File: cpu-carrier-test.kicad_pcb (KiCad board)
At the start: 2 copper layers, 99.9 x 103.3 mm, 89 parts, among them J1 Micro_SD_Card_Det, J1101 USB_miniB, J1102 USB_C_Receptacle_USB2.0, J19 SFP, J20 SFP_CAGE, J4 JTAG, J5 Molex_0936263508, J6 USB_A, SW1 SW_Push, U1 TXS0108EPW, U1101 USB3740B-AI9, U1102 UTC2000, U1103 FT232RL, U1104 74LVC1G00, U1105 SC185, U6 PCA9546AD, U8 74AC125, U9 TPS2051B

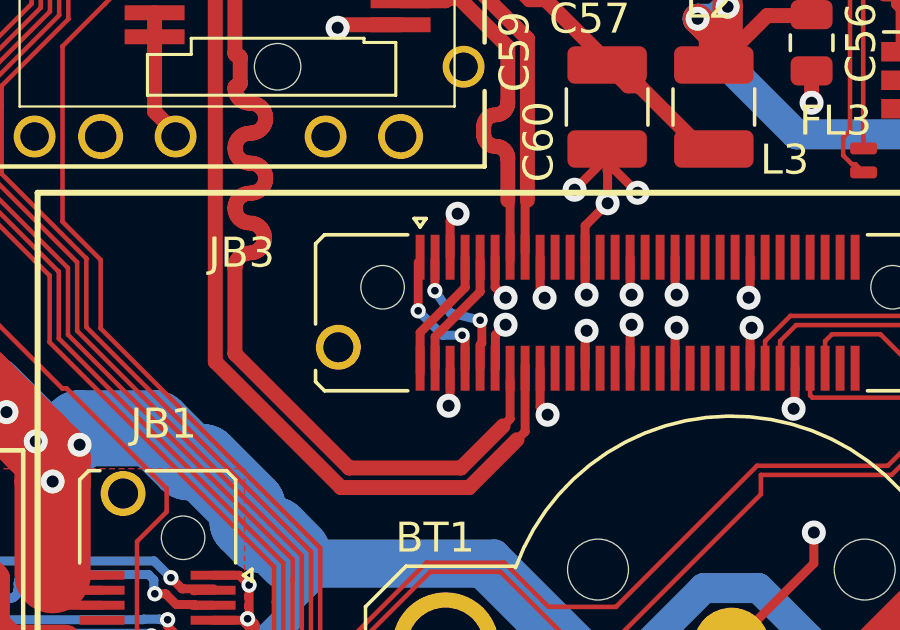
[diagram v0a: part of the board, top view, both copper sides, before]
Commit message: changed design rules to jlcpcb 4-layer setup; started reworking diff-pairs
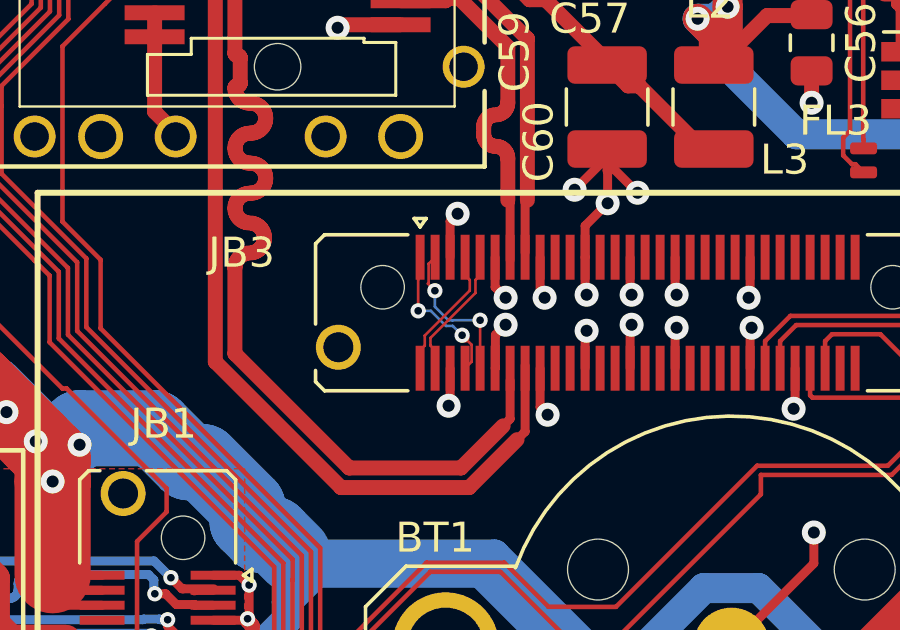
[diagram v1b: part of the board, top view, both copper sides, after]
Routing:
- net /B2B Connector/MGT_TX0_P: track 4.58 -> 5.22 mm
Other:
- copper layers 2 -> 4
- net class Default: trace_width 0.153 -> 0.1524
- net class diffp: clearance 0.1778 -> 0.0889; trace_width 0.2794 -> 0.0889; via_dia 0.508 -> 0.46; via_drill 0.254 -> 0.2
- rule trace_min: 0.153 -> 0.0889
- rule via_min_drill: 0.254 -> 0.2
- rule via_min_size: 0.508 -> 0.46

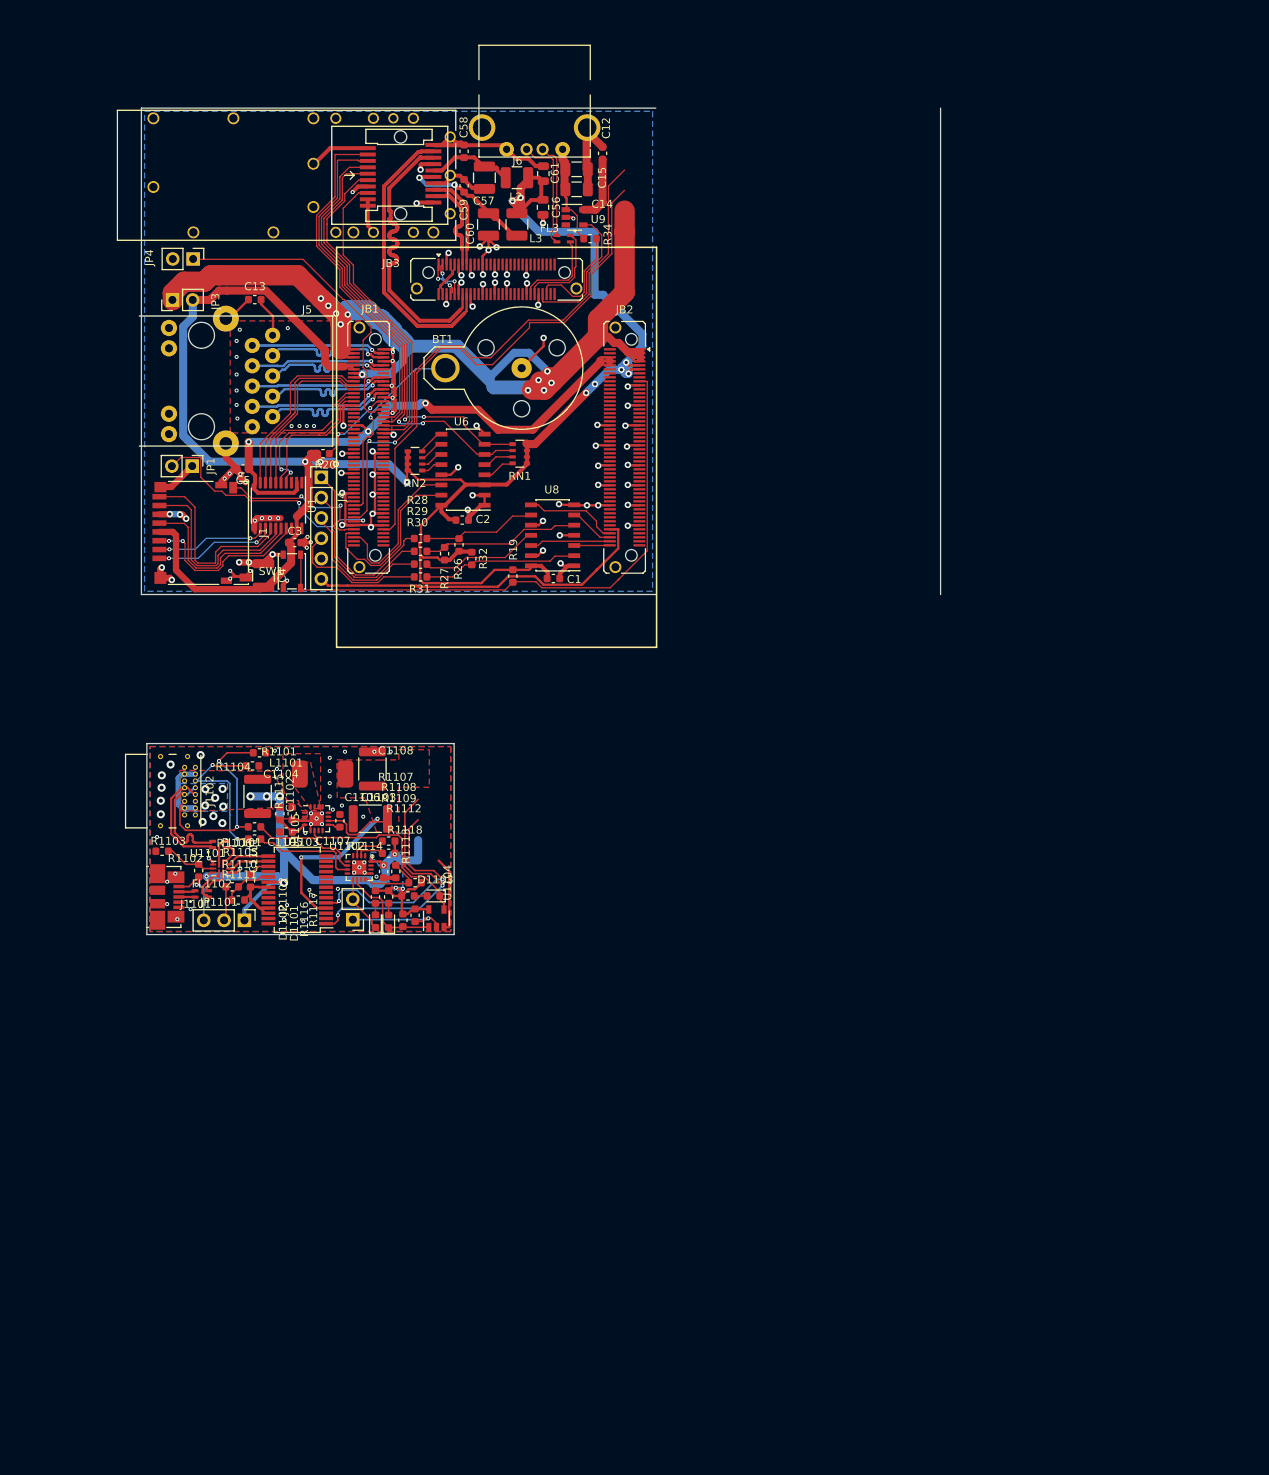
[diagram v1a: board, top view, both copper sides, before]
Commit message: added gnd and 3V3 layers; redrew board edge and placed power module
The power module is still unconnected
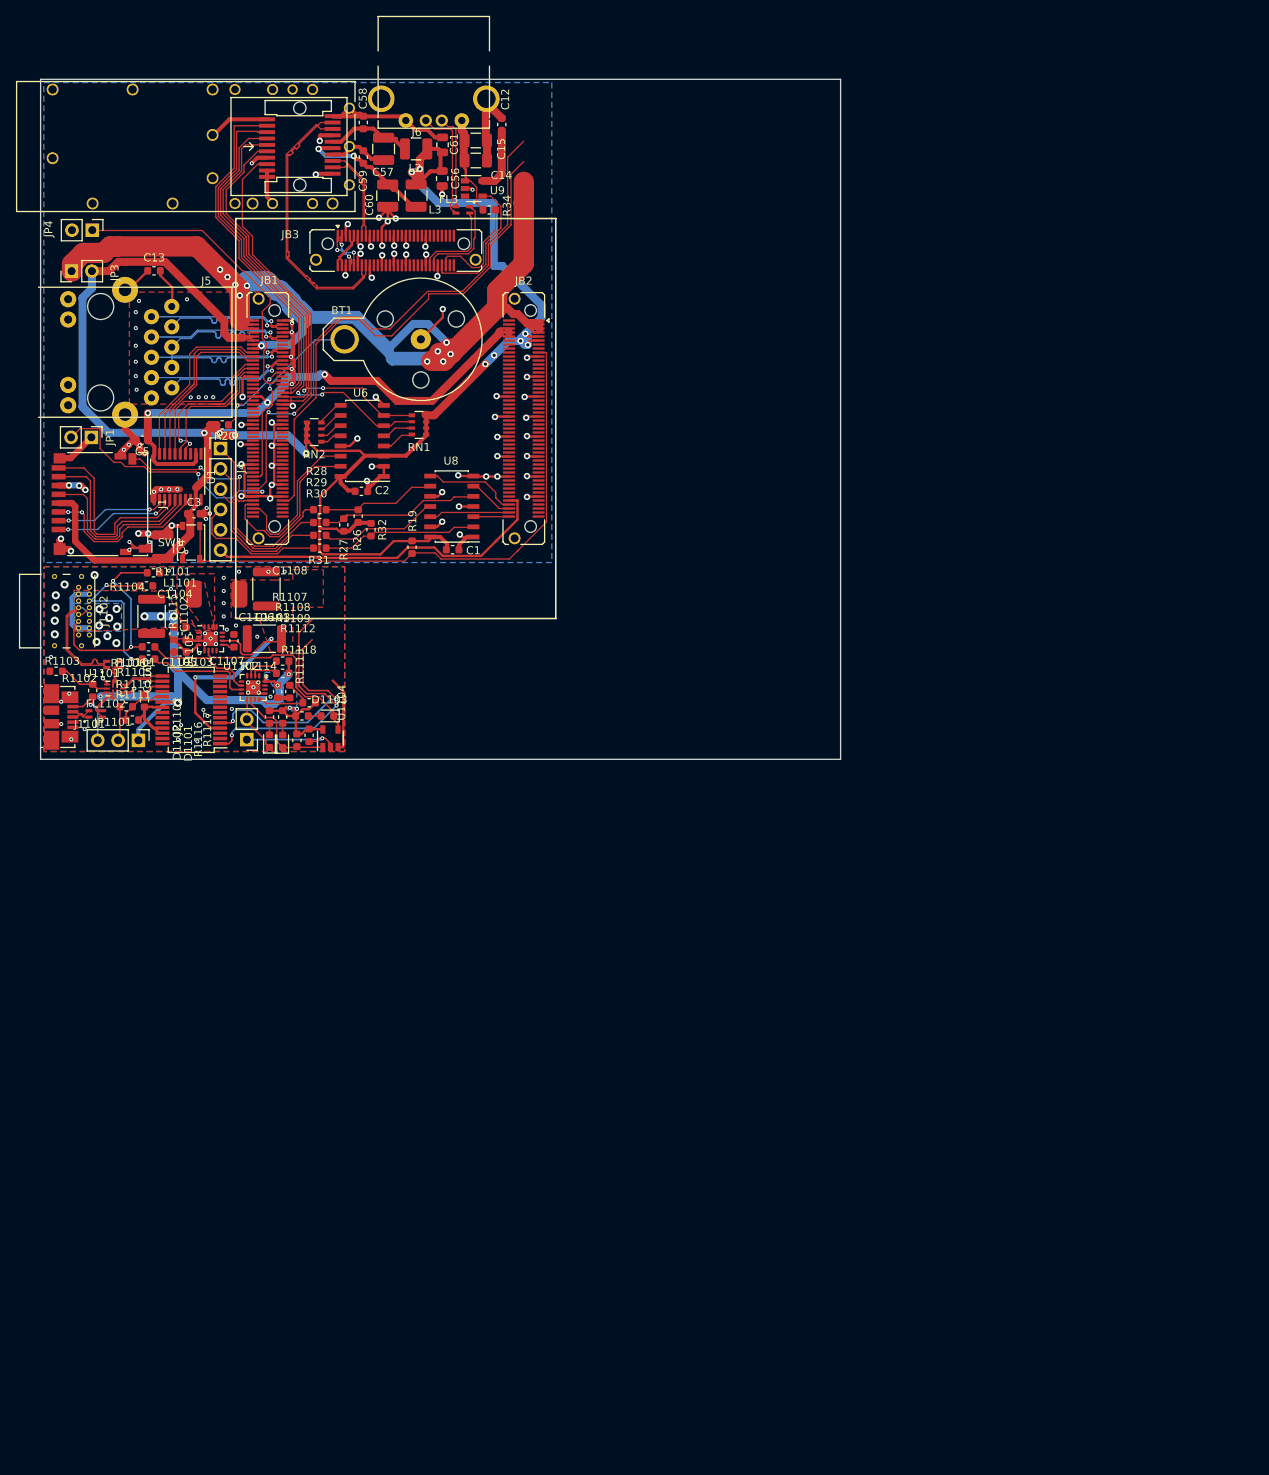
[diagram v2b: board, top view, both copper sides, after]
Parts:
- moved U1103 26.1 mm to (118.8, 108.8)
- moved C1101 26.1 mm to (113.0, 107.7)
- moved C1103 26.1 mm to (129.6, 106.5)
- moved D1103 26.1 mm to (135.8, 109.6)
- moved R1109 26.1 mm to (131.1, 106.5)
- moved R1110 26.1 mm to (110.7, 108.4)
- moved R1118 26.1 mm to (132.7, 109.6)
- moved U1101 26.1 mm to (109.3, 106.2)
- moved C1102 26.1 mm to (118.2, 99.3)
- moved C1104 26.1 mm to (113.9, 97.1)
- moved C1108 26.1 mm to (128.2, 93.7)
- moved D1101 26.1 mm to (130.3, 112.8)
- moved D1102 26.1 mm to (128.6, 112.7)
- moved FL1101 26.1 mm to (109.1, 103.2)
- moved FL1102 26.1 mm to (106.9, 109.3)
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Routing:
- net +5V: track 96.8 -> 91.1 mm
- net PHY_MDIO1_N: track 17.0 -> 19.8 mm
- net MGT_TX1_N: track 37.0 -> 34.6 mm
- net MGT_TX1_P: track 36.9 -> 34.6 mm
- net /power-and-uart/Sheet5C4CE702/USB2_N: track 3.60 -> 4.66 mm
- net /power-and-uart/Sheet5C4CE702/USB1_N: track 3.47 -> 2.71 mm
- added copper zone on In2.Cu, net +3V3
- added copper zone on In1.Cu, net OTG_ID
- added copper zone on In2.Cu, net OTG_ID
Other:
- board size 99.9 x 103.3 mm -> 100 x 85 mm

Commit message: don't remember changes :-(
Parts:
- added H1: MountingHole_Pad, MountingHole:MountingHole_3.2mm_M3_ISO14580_Pad_TopBottom, F.Cu at (161.4, 50.4)
- added H2: MountingHole_Pad, MountingHole:MountingHole_3.2mm_M3_ISO14580_Pad_TopBottom, F.Cu at (161.4, 94.4)
- added H3: MountingHole_Pad, MountingHole:MountingHole_3.2mm_M3_ISO14580_Pad_TopBottom, F.Cu at (127.4, 50.4)
- added H4: MountingHole_Pad, MountingHole:MountingHole_3.2mm_M3_ISO14580_Pad_TopBottom, F.Cu at (127.4, 94.4)
- moved J1101 120.7 mm to (197.4, 35.0), turned to 90 degrees
- moved R1103 115.1 mm to (198.1, 40.8), turned to 180 degrees
- moved FL1102 113.6 mm to (193.1, 35.4), turned to 180 degrees
- moved R1102 110.4 mm to (193.5, 38.3), turned to 90 degrees
- moved JP1101 110.4 mm to (187.8, 32.1), turned to 90 degrees
- moved R1111 107.8 mm to (188.5, 34.7), turned to 180 degrees
- moved R1110 106.7 mm to (189.3, 36.3), turned to 180 degrees
- moved U1101 105.8 mm to (190.7, 38.6), turned to 90 degrees
- moved FL1101 102.4 mm to (190.9, 41.6), turned to 180 degrees
- moved C1101 102.3 mm to (187.0, 37.1), turned to 90 degrees
- moved J1102 97.4 mm to (193.9, 51.2), turned to 90 degrees
- moved U1103 95.9 mm to (181.2, 35.9), turned to 0 degrees
- moved R1105 94.6 mm to (186.5, 42.3), turned to 180 degrees
- moved JP1102 93.8 mm to (174.2, 32.2), turned to 0 degrees
- moved R1106 92.7 mm to (186.5, 43.8), turned to 180 degrees
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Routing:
- net +3V3_PWR_OUT: track 205.6 -> 188.3 mm
- net B13_L4_N: track 38.1 -> 37.1 mm
- net MGT_TX1_P: track 34.6 -> 35.6 mm
- net MGT_TX1_N: track 34.6 -> 35.6 mm
- net SDA1: track 57.5 -> 58.2 mm
- net B13_L4_P: track 40.6 -> 39.9 mm
- net /B2B Connector/MODE: track 39.5 -> 39.0 mm
